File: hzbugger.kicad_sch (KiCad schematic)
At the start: 55 parts, among them J2 IDC, J4 SWD, J6 GPIO, SW1 RESET_SW, SW2 BOOT0_SW, U1 STM32F103C8T6, U2 SRV05-4, U3 AMS1117-3.3, U4 HX AM 90D, Y1 8M

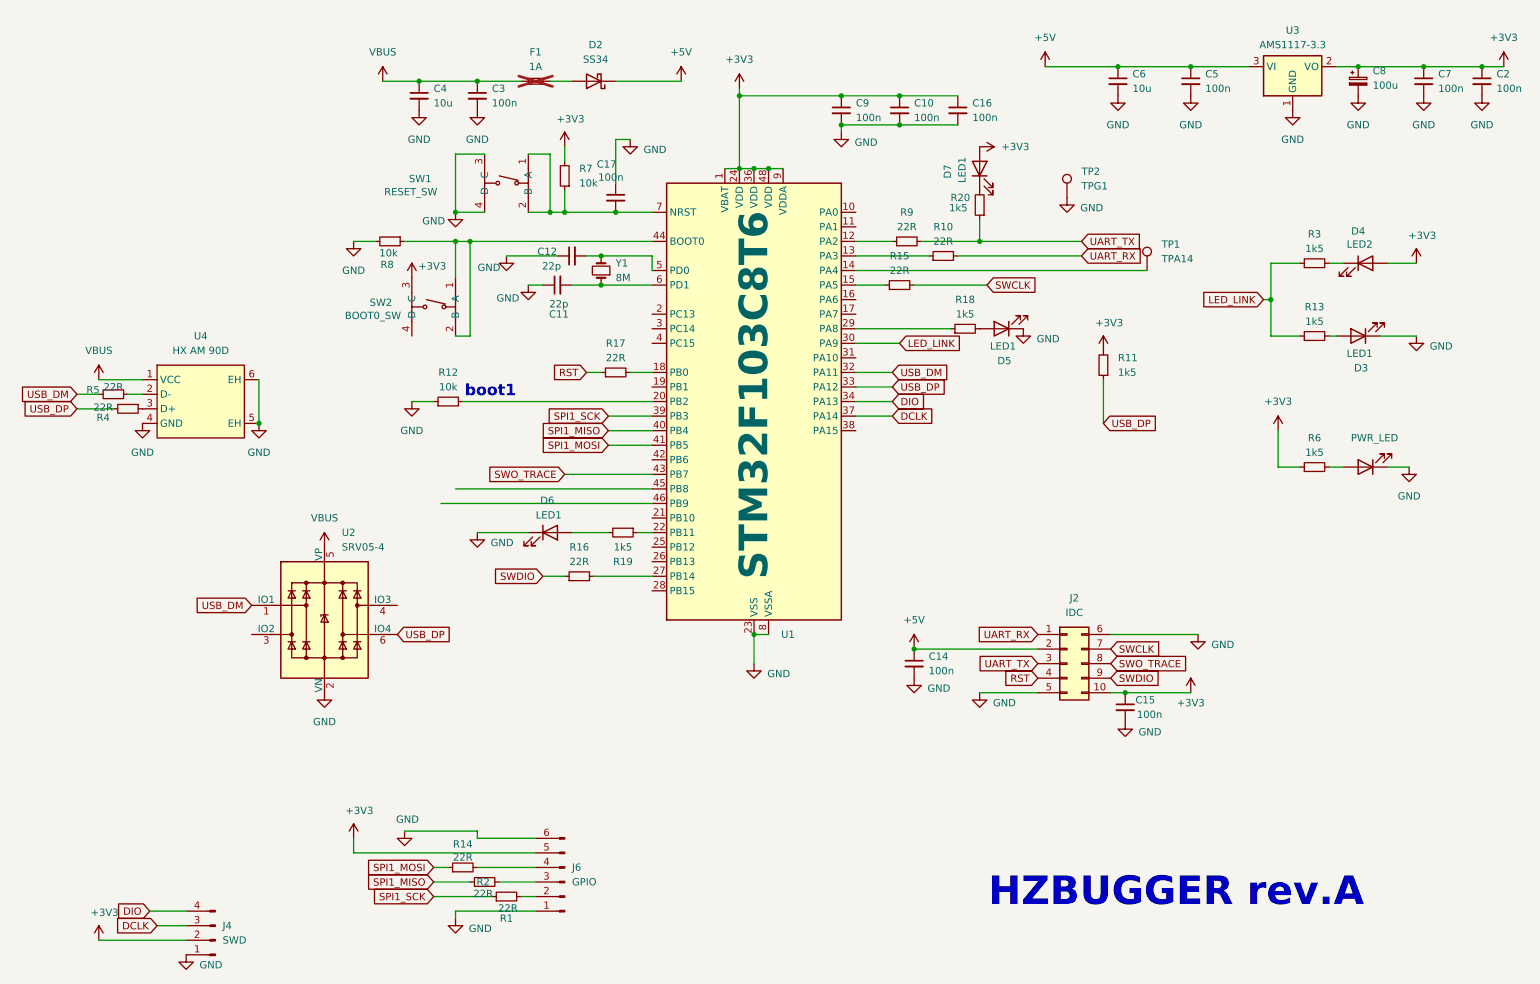
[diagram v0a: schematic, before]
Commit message: pinout enhancements, layout, physical outline + gitignore updateg
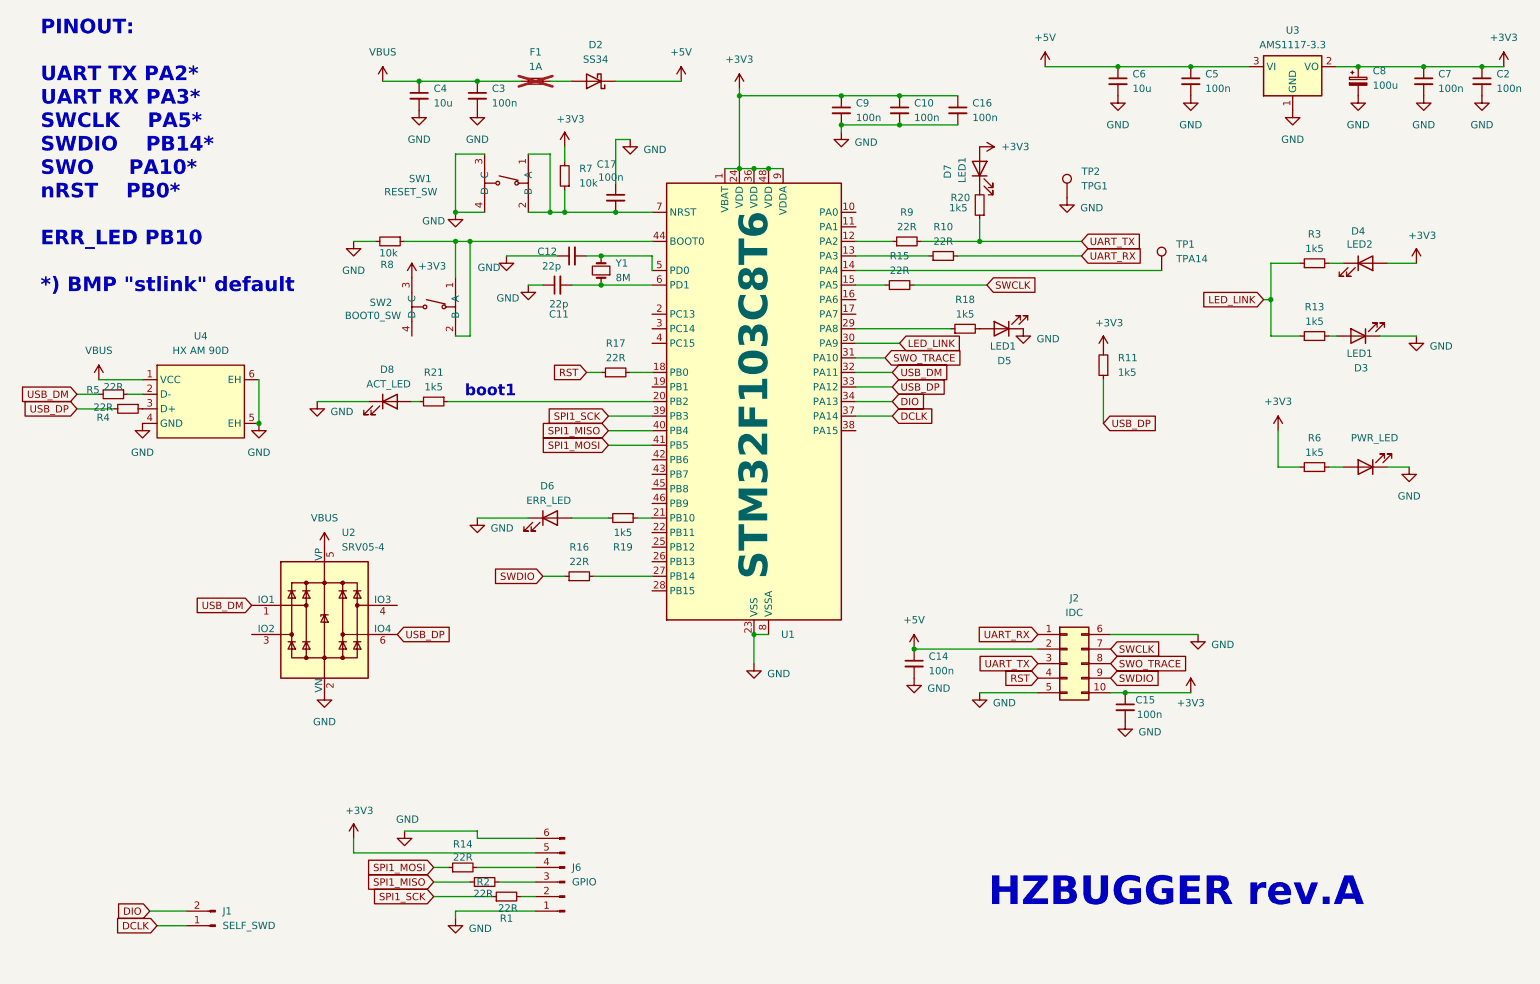
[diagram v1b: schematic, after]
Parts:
- removed J4: SWD, hzbugger:SMD-PinHeader_1x04_P2.54mm_Vertical, symbol Connector:Conn_01x04_Pin
- removed R12: 10k, Resistor_SMD:R_0402_1005Metric, symbol Device:R_Small
- added D8: ACT_LED, LED_SMD:LED_0805_2012Metric, symbol Device:LED
- added J1: SELF_SWD, Connector_PinHeader_2.54mm:PinHeader_1x02_P2.54mm_Vertical, symbol Connector:Conn_01x02_Pin
- added R21: 1k5, Resistor_SMD:R_0402_1005Metric, symbol Device:R_Small
- D6: value LED1 -> ERR_LED
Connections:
- net DCLK: now also J1.1 (Pin_1)
- net DIO: now also J1.2 (Pin_2)
- net GND: now also D8.1 (K)
- net SWO_TRACE: now also U1.31 (PA10); no longer U1.43 (PB7)
- net at U1.20 (PB2): now also R21.1
- net at R19.1: now also U1.21 (PB10); no longer U1.22 (PB11)
- new net: D8.2 (A), R21.2
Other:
- note added: "PINOUT: UART TX PA2* UART RX PA3* SWCLK PA5* SWDIO PB14* SWO PA10* nRST PB0* ERR_LED PB10 *) BMP "stlink" default"
- moved on the sheet: D6, R19, TP1

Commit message: form factor, mounting holes
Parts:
- added H1: MountingHole, MountingHole:MountingHole_2.1mm, symbol Mechanical:MountingHole
- added H2: MountingHole_Pad, MountingHole:MountingHole_2.1mm, symbol Mechanical:MountingHole
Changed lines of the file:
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@@
 		(effects
 			(font
+				(face "KiCad Font")
 				(size 2.54 2.54)
 				(thickness 0.254)
@@
 	(wire
 		(pts
-			(xy 242.57 100.33) (xy 245.11 100.33)
+			(xy 116.84 91.44) (xy 124.46 91.44)
 		)
 		(stroke
@@
 	(wire
 		(pts
-			(xy 116.84 91.44) (xy 124.46 91.44)
+			(xy 242.57 100.33) (xy 245.11 100.33)
 		)
 		(stroke
@@
 	)
 	(symbol
+		(lib_id "Mechanical:MountingHole")
+		(at 135.89 166.37 0)
+		(unit 1)
+		(body_style 1)
+		(exclude_from_sim no)
+		(in_bom no)
+		(on_board yes)
+		(in_pos_files yes)
+		(dnp no)
+		(fields_autoplaced yes)
+		(property "Reference" "H1"
+			(at 138.43 165.0999 0)
+			(show_name no)
+			(do_not_autoplace no)
+			(effects
+				(font
+					(size 1.27 1.27)
+				)
+				(justify left)
+			)
+		)
+		(property "Value" "MountingHole"
+			(at 138.43 167.6399 0)
+			(show_name no)
+			(do_not_autoplace no)
+			(effects
+				(font
+					(size 1.27 1.27)
+				)
+				(justify left)
+			)
+		)
+		(property "Footprint" "MountingHole:MountingHole_2.1mm"
+			(at 135.89 166.37 0)
+			(hide yes)
+			(show_name no)
+			(do_not_autoplace no)
+			(effects
+				(font
+					(size 1.27 1.27)
+				)
+			)
+		)
+		(property "Datasheet" ""
+			(at 135.89 166.37 0)
+			(hide yes)
+			(show_name no)
+			(do_not_autoplace no)
+			(effects
+				(font
+					(size 1.27 1.27)
+				)
+			)
+		)
+		(property "Description" "Mounting Hole without connection"
+			(at 135.89 166.37 0)
+			(hide yes)
+			(show_name no)
+			(do_not_autoplace no)
+			(effects
+				(font
+					(size 1.27 1.27)
+				)
+			)
+		)
+		(instances
+			(project "hzbugger"
+				(path "/493ccddd-ac13-43bb-97a7-ed9a2ed970cc"
+					(reference "H1")
+					(unit 1)
+				)
+			)
+		)
+	)
+	(symbol
 		(lib_id "Connector:TestPoint")
 		(at 213.36 66.04 0)
@@
 					(unit 1)
 				)
+			)
+		)
+	)
+	(symbol
+		(lib_id "Mechanical:MountingHole")
+		(at 135.89 179.07 0)
+		(unit 1)
+		(body_style 1)
+		(exclude_from_sim no)
+		(in_bom no)
+		(on_board yes)
+		(in_pos_files yes)
+		(dnp no)
+		(fields_autoplaced yes)
+		(property "Reference" "H2"
+			(at 138.43 177.7999 0)
+			(show_name no)
+			(do_not_autoplace no)
+			(effects
+				(font
+					(size 1.27 1.27)
+				)
+				(justify left)
+			)
+		)
+		(property "Value" "MountingHole_Pad"
+			(at 138.43 180.3399 0)
+			(show_name no)
+			(do_not_autoplace no)
+			(effects
+				(font
+					(size 1.27 1.27)
+				)
+				(justify left)
+			)
+		)
+		(property "Footprint" "MountingHole:MountingHole_2.1mm"
+			(at 135.89 179.07 0)
+			(hide yes)
+			(show_name no)
+			(do_not_autoplace no)
+			(effects
+				(font
+					(size 1.27 1.27)
+				)
+			)
+		)
+		(property "Datasheet" ""
+			(at 135.89 179.07 0)
+			(hide yes)
+			(show_name no)
+			(do_not_autoplace no)
+			(effects
+				(font
+					(size 1.27 1.27)
+				)
+			)
+		)
+		(property "Description" "Mounting Hole without connection"
+			(at 135.89 179.07 0)
+			(hide yes)
+			(show_name no)
+			(do_not_autoplace no)
+			(effects
+				(font
+					(size 1.27 1.27)
+				)
+			)
+		)
+		(instances
+			(project "hzbugger"
+				(path "/493ccddd-ac13-43bb-97a7-ed9a2ed970cc"
+					(reference "H2")
+					(unit 1)
+				)
